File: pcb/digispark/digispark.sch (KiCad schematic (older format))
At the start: 17 parts, among them J1 USB_B, U1 MC78M05BDTRKG, U2 ATTINY85-20SU

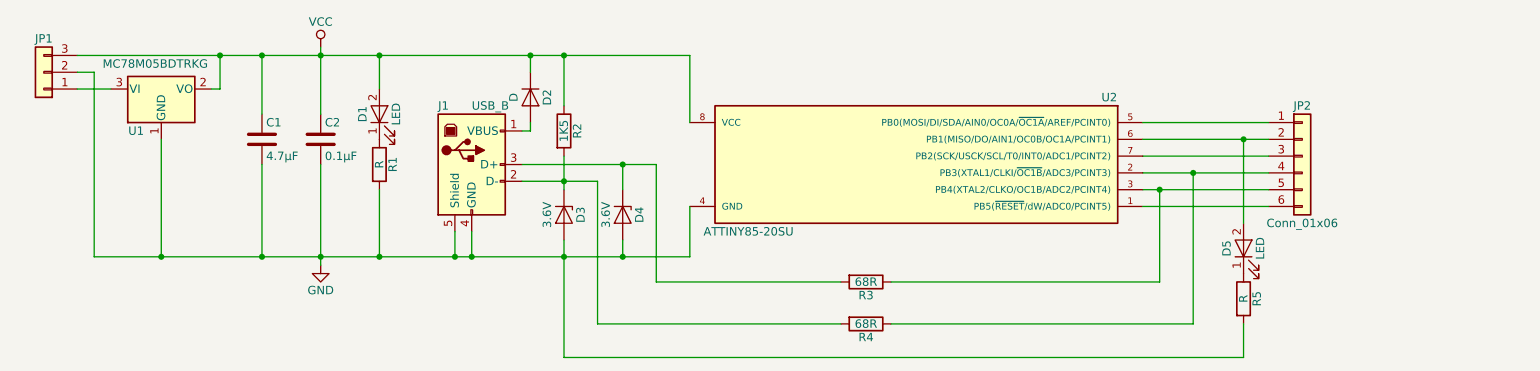
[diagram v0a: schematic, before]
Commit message: add icsp header to digispark schematic.
picture of assembled digispark as usbtinyisp
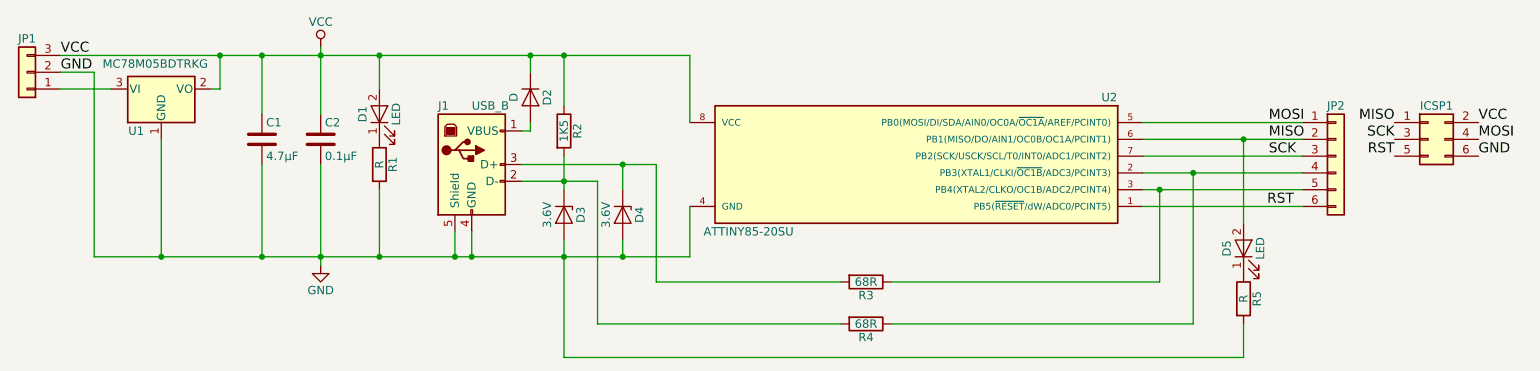
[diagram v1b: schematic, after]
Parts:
- added ICSP1: Conn_02x03_Odd_Even, symbol Conn_02x03_Odd_Even
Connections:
- net GND: now also ICSP1.6 (Pin_6)
- net VCC: now also ICSP1.2 (Pin_2)
- net RST: now reaches JP2.6 (Pin_6), U2.1 (PB5(~RESET~/dW/ADC0/PCINT5))
- net RST: now also ICSP1.5 (Pin_5)
- net MOSI: now reaches JP2.1 (Pin_1), U2.5 (PB0(MOSI/DI/SDA/AIN0/OC0A/~OC1A~/AREF/PCINT0))
- net MOSI: now also ICSP1.4 (Pin_4)
- net MISO: now reaches D5.2 (A), JP2.2 (Pin_2), U2.6 (PB1(MISO/DO/AIN1/OC0B/OC1A/PCINT1))
- net MISO: now also ICSP1.1 (Pin_1)
- net SCK: now reaches JP2.3 (Pin_3), U2.7 (PB2(SCK/USCK/SCL/T0/INT0/ADC1/PCINT2))
- net SCK: now also ICSP1.3 (Pin_3)
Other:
- moved on the sheet: JP1, JP2
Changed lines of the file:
@@
 LIBS:contrib
 LIBS:valves
+LIBS:digispark-cache
 EELAYER 25 0
 EELAYER END
@@
 L Conn_01x03 JP1
 U 1 1 5AE1E838
-P 1950 3700
-F 0 "JP1" H 1950 3500 50  0000 C CNN
-F 1 "Conn_01x03" H 1950 3900 50  0001 C CNN
-F 2 "" H 1950 3700 50  0001 C CNN
-F 3 "" H 1950 3700 50  0001 C CNN
-	1    1950 3700
+P 1850 3700
+F 0 "JP1" H 1850 3500 50  0000 C CNN
+F 1 "Conn_01x03" H 1850 3900 50  0001 C CNN
+F 2 "" H 1850 3700 50  0001 C CNN
+F 3 "" H 1850 3700 50  0001 C CNN
+	1    1850 3700
 	-1   0    0    1
 $EndComp
 Wire Wire Line
-	2150 3800 2350 3800
+	2050 3800 2350 3800
 $Comp
 L GND #PWR2
@@
 $EndComp
 Wire Wire Line
-	2150 3700 2250 3700
+	2050 3700 2250 3700
 $Comp
 L VCC #PWR1
@@
 Connection ~ 3250 3600
 Wire Wire Line
-	2150 3600 3000 3600
+	2050 3600 3000 3600
 Wire Wire Line
 	3000 3600 3250 3600
@@
 $EndComp
 Wire Wire Line
-	8500 4000 9250 4000
+	8500 4000 9450 4000
 Wire Wire Line
 	8500 4100 9100 4100
 Wire Wire Line
-	9100 4100 9250 4100
-Wire Wire Line
-	8500 4200 9250 4200
+	9100 4100 9450 4100
+Wire Wire Line
+	8500 4200 9450 4200
 Wire Wire Line
 	8500 4300 8800 4300
 Wire Wire Line
-	8800 4300 9250 4300
+	8800 4300 9450 4300
 Wire Wire Line
 	8500 4400 8600 4400
 Wire Wire Line
-	8600 4400 9250 4400
+	8600 4400 9450 4400
 $Comp
 L Conn_01x06 JP2
 U 1 1 5AE2076C
-P 9450 4200
-F 0 "JP2" H 9450 4500 50  0000 C CNN
-F 1 "Conn_01x06" H 9450 3800 50  0000 C CNN
-F 2 "" H 9450 4200 50  0001 C CNN
-F 3 "" H 9450 4200 50  0001 C CNN
-	1    9450 4200
-	1    0    0    -1
-$EndComp
-Wire Wire Line
-	8500 4500 9250 4500
+P 9650 4200
+F 0 "JP2" H 9650 4500 50  0000 C CNN
+F 1 "Conn_01x06" H 9650 3800 50  0001 C CNN
+F 2 "" H 9650 4200 50  0001 C CNN
+F 3 "" H 9650 4200 50  0001 C CNN
+	1    9650 4200
+	1    0    0    -1
+$EndComp
+Wire Wire Line
+	8500 4500 9450 4500
 Wire Wire Line
 	8600 4400 8600 4950
@@
 Wire Wire Line
 	3000 3800 2950 3800
+$Comp
+L Conn_02x03_Odd_Even ICSP1
+U 1 1 5AE278E3
+P 10200 4100
+F 0 "ICSP1" H 10250 4300 50  0000 C CNN
+F 1 "Conn_02x03_Odd_Even" H 10250 3900 50  0001 C CNN
+F 2 "" H 10200 4100 50  0001 C CNN
+F 3 "" H 10200 4100 50  0001 C CNN
+	1    10200 4100
+	1    0    0    -1
+$EndComp
+Text Label 10000 4000 2    60   ~ 0
+MISO
+Text Label 10000 4100 2    60   ~ 0
+SCK
+Text Label 10000 4200 2    60   ~ 0
+RST
+Text Label 9400 4500 2    60   ~ 0
+RST
+Text Label 10500 4200 0    60   ~ 0
+GND
+Text Label 10500 4100 0    60   ~ 0
+MOSI
+Text Label 10500 4000 0    60   ~ 0
+VCC
+Text Label 2050 3600 0    60   ~ 0
+VCC
+Text Label 2050 3700 0    60   ~ 0
+GND
+Text Label 9250 4000 0    60   ~ 0
+MOSI
+Text Label 9250 4100 0    60   ~ 0
+MISO
+Text Label 9250 4200 0    60   ~ 0
+SCK
 $EndSCHEMATC
